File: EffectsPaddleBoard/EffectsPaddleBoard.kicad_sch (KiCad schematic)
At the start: 45 parts, among them J3 Barrel_Jack, U2 TPS54233, U4 TPS54233

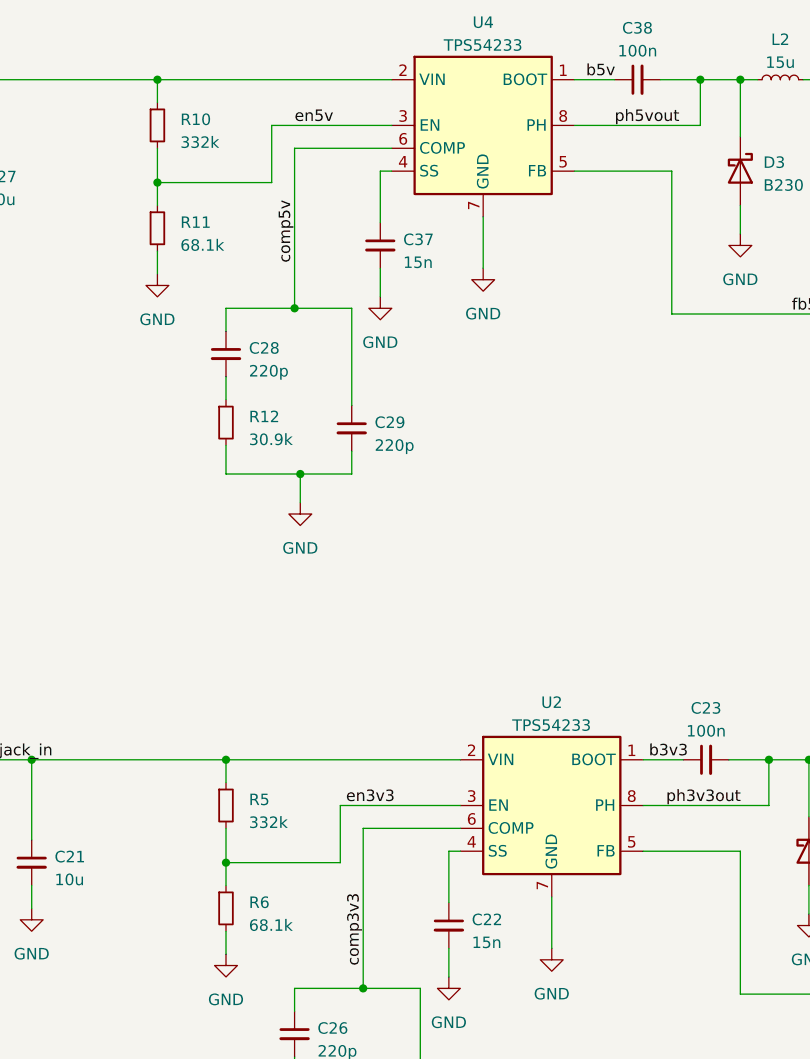
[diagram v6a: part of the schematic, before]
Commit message: Proceeded in layout, just power is missing
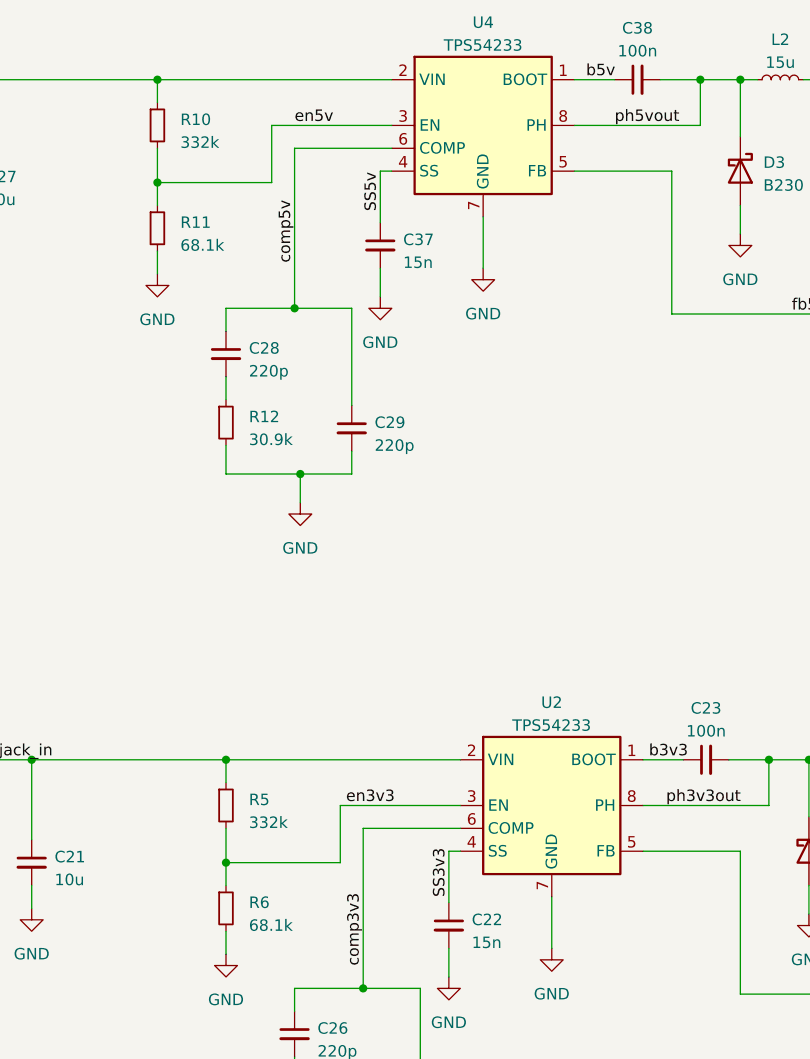
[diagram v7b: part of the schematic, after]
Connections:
- net SS3v3: now reaches C22.1, U2.4 (SS)
- net SS5v: now reaches C37.1, U4.4 (SS)
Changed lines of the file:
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@@
+    (effects (font (size 1.27 1.27)) (justify left bottom))
+  )
+  (label "SS3v3" (at 117.475 125.095 90) (fields_autoplaced)
     (effects (font (size 1.27 1.27)) (justify left bottom))
   )
@@
     (effects (font (size 1.27 1.27)) (justify left bottom))
   )
+  (label "SS5v" (at 109.855 48.895 90) (fields_autoplaced)
+    (effects (font (size 1.27 1.27)) (justify left bottom))
+  )

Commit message: Finished layout
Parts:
- added D1: LED, LED_SMD:LED_0402_1005Metric, symbol Device:LED
- added R2: 220, Resistor_SMD:R_0402_1005Metric, symbol Device:R
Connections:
- net +3.3V: now also R2.2
- net GND: now also D1.1 (K)
- new net: D1.2 (A), R2.1
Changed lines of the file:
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@@
+    (stroke (width 0) (type default))
+  )
+  (wire (pts (xy 18.415 57.785) (xy 18.415 63.5))
     (stroke (width 0) (type default))
   )
@@
     (stroke (width 0) (type default))
   )
+  (wire (pts (xy 18.415 63.5) (xy 22.225 63.5))
+    (stroke (width 0) (type default))
+  )
   (wire (pts (xy 148.59 109.855) (xy 153.035 109.855))
     (stroke (width 0) (type default))
@@
     (stroke (width 0) (type default))
   )
+  (wire (pts (xy 38.1 63.5) (xy 38.1 69.85))
+    (stroke (width 0) (type default))
+  )
   (wire (pts (xy 100.33 135.255) (xy 100.33 137.795))
     (stroke (width 0) (type default))
@@
     (stroke (width 0) (type default))
   )
+  (wire (pts (xy 29.845 63.5) (xy 38.1 63.5))
+    (stroke (width 0) (type default))
+  )
   (wire (pts (xy 177.8 69.85) (xy 177.8 71.12))
     (stroke (width 0) (type default))
@@
   )
   (wire (pts (xy 48.26 114.935) (xy 42.545 114.935))
+    (stroke (width 0) (type default))
+  )
+  (wire (pts (xy 38.1 77.47) (xy 38.1 82.55))
     (stroke (width 0) (type default))
   )
@@
     )
   )
+  (symbol (lib_id "Device:LED") (at 38.1 73.66 90) (unit 1)
+    (in_bom yes) (on_board yes) (dnp no) (fields_autoplaced)
+    (property "Reference" "D1" (at 41.91 74.6125 90)
+      (effects (font (size 1.27 1.27)) (justify right))
+    )
+    (property "Value" "LED" (at 41.91 77.1525 90)
+      (effects (font (size 1.27 1.27)) (justify right))
+    )
+    (property "Footprint" "LED_SMD:LED_0402_1005Metric" (at 38.1 73.66 0)
+      (effects (font (size 1.27 1.27)) hide)
+    )
+    (property "Datasheet" "~" (at 38.1 73.66 0)
+      (effects (font (size 1.27 1.27)) hide)
+    )
+    (property "Sim.Enable" "0" (at 38.1 73.66 0)
+      (effects (font (size 1.27 1.27)) hide)
+    )
+    (pin "1")
+    (pin "2")
+    (instances
+      (project "EffectsPaddleBoard"
+        (path "/40bb1606-5207-4492-95b9-876879aab2b4/430de8a6-c174-447f-a683-0bfbe392d7bf"
+          (reference "D1") (unit 1)
+        )
+        (path "/40bb1606-5207-4492-95b9-876879aab2b4"
+          (reference "D4") (unit 1)
+        )
+      )
+    )
+  )
   (symbol (lib_id "Device:C_Polarized") (at 34.29 181.61 0) (unit 1)
     (in_bom yes) (on_board yes) (dnp no) (fields_autoplaced)
@@
         (path "/40bb1606-5207-4492-95b9-876879aab2b4"
           (reference "R7") (unit 1)
+        )
+      )
+    )
+  )
+  (symbol (lib_id "Device:R") (at 26.035 63.5 270) (unit 1)
+    (in_bom yes) (on_board yes) (dnp no) (fields_autoplaced)
+    (property "Reference" "R2" (at 26.035 58.42 90)
+      (effects (font (size 1.27 1.27)))
+    )
+    (property "Value" "220" (at 26.035 60.96 90)
+      (effects (font (size 1.27 1.27)))
+    )
+    (property "Footprint" "Resistor_SMD:R_0402_1005Metric" (at 26.035 61.722 90)
+      (effects (font (size 1.27 1.27)) hide)
+    )
+    (property "Datasheet" "~" (at 26.035 63.5 0)
+      (effects (font (size 1.27 1.27)) hide)
+    )
+    (property "Sim.Enable" "0" (at 26.035 63.5 0)
+      (effects (font (size 1.27 1.27)) hide)
+    )
+    (pin "1")
+    (pin "2")
+    (instances
+      (project "EffectsPaddleBoard"
+        (path "/40bb1606-5207-4492-95b9-876879aab2b4/430de8a6-c174-447f-a683-0bfbe392d7bf"
+          (reference "R2") (unit 1)
+        )
+        (path "/40bb1606-5207-4492-95b9-876879aab2b4"
+          (reference "R32") (unit 1)
         )
       )
@@
     )
   )
+  (symbol (lib_id "power:GND") (at 38.1 82.55 0) (unit 1)
+    (in_bom yes) (on_board yes) (dnp no) (fields_autoplaced)
+    (property "Reference" "#PWR07" (at 38.1 88.9 0)
+      (effects (font (size 1.27 1.27)) hide)
+    )
+    (property "Value" "GND" (at 38.1 87.63 0)
+      (effects (font (size 1.27 1.27)))
+    )
+    (property "Footprint" "" (at 38.1 82.55 0)
+      (effects (font (size 1.27 1.27)) hide)
+    )
+    (property "Datasheet" "" (at 38.1 82.55 0)
+      (effects (font (size 1.27 1.27)) hide)
+    )
+    (property "Sim.Enable" "0" (at 38.1 82.55 0)
+      (effects (font (size 1.27 1.27)) hide)
+    )
+    (pin "1")
+    (instances
+      (project "EffectsPaddleBoard"
+        (path "/40bb1606-5207-4492-95b9-876879aab2b4/430de8a6-c174-447f-a683-0bfbe392d7bf"
+          (reference "#PWR07") (unit 1)
+        )
+        (path "/40bb1606-5207-4492-95b9-876879aab2b4"
+          (reference "#PWR085") (unit 1)
+        )
+      )
+    )
+  )
   (symbol (lib_id "power:GND") (at 121.285 55.245 0) (unit 1)
     (in_bom yes) (on_board yes) (dnp no) (fields_autoplaced)
@@
         )
       )
+    )
+  )
+  (symbol (lib_id "power:+3.3V") (at 18.415 57.785 0) (unit 1)
+    (in_bom yes) (on_board yes) (dnp no) (fields_autoplaced)
+    (property "Reference" "#PWR01" (at 18.415 61.595 0)
+      (effects (font (size 1.27 1.27)) hide)
+    )
+    (property "Value" "+3.3V" (at 18.415 53.975 0)
+      (effects (font (size 1.27 1.27)))
+    )
+    (property "Footprint" "" (at 18.415 57.785 0)
+      (effects (font (size 1.27 1.27)) hide)
+    )
+    (property "Datasheet" "" (at 18.415 57.785 0)
+      (effects (font (size 1.27 1.27)) hide)
+    )
+    (property "Sim.Enable" "0" (at 18.415 57.785 0)
+      (effects (font (size 1.27 1.27)) hide)
+    )
+    (pin "1")
+    (instances
+      (project "EffectsPaddleBoard"
+        (path "/40bb1606-5207-4492-95b9-876879aab2b4/430de8a6-c174-447f-a683-0bfbe392d7bf"
+          (reference "#PWR01") (unit 1)
+        )
+        (path "/40bb1606-5207-4492-95b9-876879aab2b4"
+          (reference "#PWR084") (unit 1)
+        )
+      )
